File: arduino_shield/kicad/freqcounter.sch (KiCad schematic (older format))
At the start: 11 parts, among them J1 ICSP PICKIT, J2 USB-Serial, P1 LCD_DISPLAY_16X2, U1 PIC16F18446, Y1 Crystal 8MHz

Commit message: Updated kicad schematic
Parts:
- removed P1: LCD_DISPLAY_16X2, SIL-16, symbol LCD_DISPLAY_16X2:LCD_DISPLAY_16X2
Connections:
- wire segments 40 -> 24
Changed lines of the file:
@@
 EESchema Schematic File Version 4
-LIBS:freqcounter_16F18446-cache
+LIBS:freqcounter-cache
 EELAYER 26 0
 EELAYER END
@@
 Wire Wire Line
 	5500 2700 6900 2700
-$Comp
-L LCD_DISPLAY_16X2:LCD_DISPLAY_16X2 P1
-U 1 1 5EA1FBB9
-P 4200 4650
-F 0 "P1" H 6533 4550 50  0000 L CNN
-F 1 "LCD_DISPLAY_16X2" H 6533 4457 50  0000 L CNN
-F 2 "SIL-16" H 6533 4364 50  0000 L CNN
-F 3 "" H 4200 4650 50  0001 C CNN
-	1    4200 4650
-	1    0    0    -1
-$EndComp
 Text GLabel 5500 3000 2    40   Input ~ 0
 LCD_RS
 Text GLabel 5500 3100 2    40   Input ~ 0
 LCD_E
-Text GLabel 4700 4400 1    40   Input ~ 0
-LCD_E
-Text GLabel 4500 4400 1    40   Input ~ 0
-LCD_RS
-Wire Wire Line
-	4600 4400 4600 4100
-Wire Wire Line
-	4600 4100 4800 4100
-Wire Wire Line
-	4800 4100 4800 4400
-Wire Wire Line
-	4800 4100 4900 4100
-Wire Wire Line
-	4900 4100 4900 4400
-Connection ~ 4800 4100
-Wire Wire Line
-	4900 4100 5000 4100
-Wire Wire Line
-	5000 4100 5000 4400
-Connection ~ 4900 4100
-Wire Wire Line
-	5000 4100 5100 4100
-Wire Wire Line
-	5100 4100 5100 4400
-Connection ~ 5000 4100
-Text GLabel 4600 4000 1    40   Input ~ 0
-GND
-Wire Wire Line
-	4600 4100 4600 4000
-Connection ~ 4600 4100
-Wire Wire Line
-	4600 4100 4400 4100
-Wire Wire Line
-	4400 4100 4400 4400
-Wire Wire Line
-	5100 4100 5700 4100
-Wire Wire Line
-	5700 4100 5700 4400
-Connection ~ 5100 4100
 Text GLabel 5500 3200 2    40   Input ~ 0
 LCD_D4
@@
 Text GLabel 4500 3200 0    40   Input ~ 0
 LCD_D6
-Text GLabel 5200 4400 1    40   Input ~ 0
-LCD_D4
-Text GLabel 5300 4400 1    40   Input ~ 0
-LCD_D5
-Text GLabel 5500 4400 1    40   Input ~ 0
-LCD_D7
-Text GLabel 5400 4400 1    40   Input ~ 0
-LCD_D6
-Wire Wire Line
-	4400 4100 4200 4100
-Wire Wire Line
-	4200 4100 4200 4400
-Connection ~ 4400 4100
-Text GLabel 4300 4400 1    40   Input ~ 0
-VDD
 Wire Wire Line
 	3750 2600 4500 2600

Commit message: Updated kicad schematic
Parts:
- removed J2: USB-Serial, symbol Connector:Conn_01x04_Female
- removed R11, R12: 180, Resistor_SMD:R_0805_2012Metric_Pad1.15x1.40mm_HandSolder, symbol Device:R
- removed U1: PIC16F18446, Package_SO:SOIC-20W_7.5x12.8mm_P1.27mm, symbol PIC16F18446:PIC16F18446
- removed Y1: Crystal 8MHz, Crystal:Crystal_HC18-U_Vertical, symbol Device:Crystal
- added C1: 10uF, Capacitor_SMD:C_0805_2012Metric_Pad1.15x1.40mm_HandSolder, symbol Device:C
- added C4, C5: 100nF, Capacitor_SMD:C_0805_2012Metric_Pad1.15x1.40mm_HandSolder, symbol Device:C
- added J10: I2C_2, symbol Connector:Conn_01x04_Male
- added J11: PARALEL, symbol Connector:Conn_01x08_Male
- added J2: Arduino_Power, symbol Connector:Conn_01x06_Male
- added J3: Arduino_Digital_2, symbol Connector:Conn_01x08_Male
- added J4: Arduino_Analog, symbol Connector:Conn_01x06_Male
- added J5: Arduino_Digital_1, symbol Connector:Conn_01x08_Male
- added J6: INPUT_A, symbol Connector:Conn_01x02_Male
- added J7: INPUT_B, symbol Connector:Conn_01x02_Male
- added J8: INPUT_ZCD, symbol Connector:Conn_01x02_Male
- added J9: I2C_1, symbol Connector:Conn_01x04_Male
- added R1: 10K, Resistor_SMD:R_0805_2012Metric_Pad1.15x1.40mm_HandSolder, symbol Device:R
- added R2: 180, Resistor_SMD:R_0805_2012Metric_Pad1.15x1.40mm_HandSolder, symbol Device:R
- added R4: 1M, Resistor_SMD:R_0805_2012Metric_Pad1.15x1.40mm_HandSolder, symbol Device:R
- added U1: PIC16F18446, symbol freqcounter:PIC16F18446
- added U2: TCXO, symbol freqcounter:TCXO
- renumbered C5 to C2, C1 to C3, R1 to R3
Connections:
- net labels added: 3.3V, 32MHz, 5V, ARD_RX, ARD_TX, ARD_VIN, AREF, P0, P1, P2, P3, RESET, SCL, SDA
- net labels removed: LCD_D4, LCD_D5, LCD_D6, LCD_D7, LCD_E, LCD_RS, RX, TX
- wire segments 24 -> 53
- no-connect marks 0 -> 1
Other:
- note added: "ARDUINO INTERFACE"
- moved on the sheet: D1, J1, R3

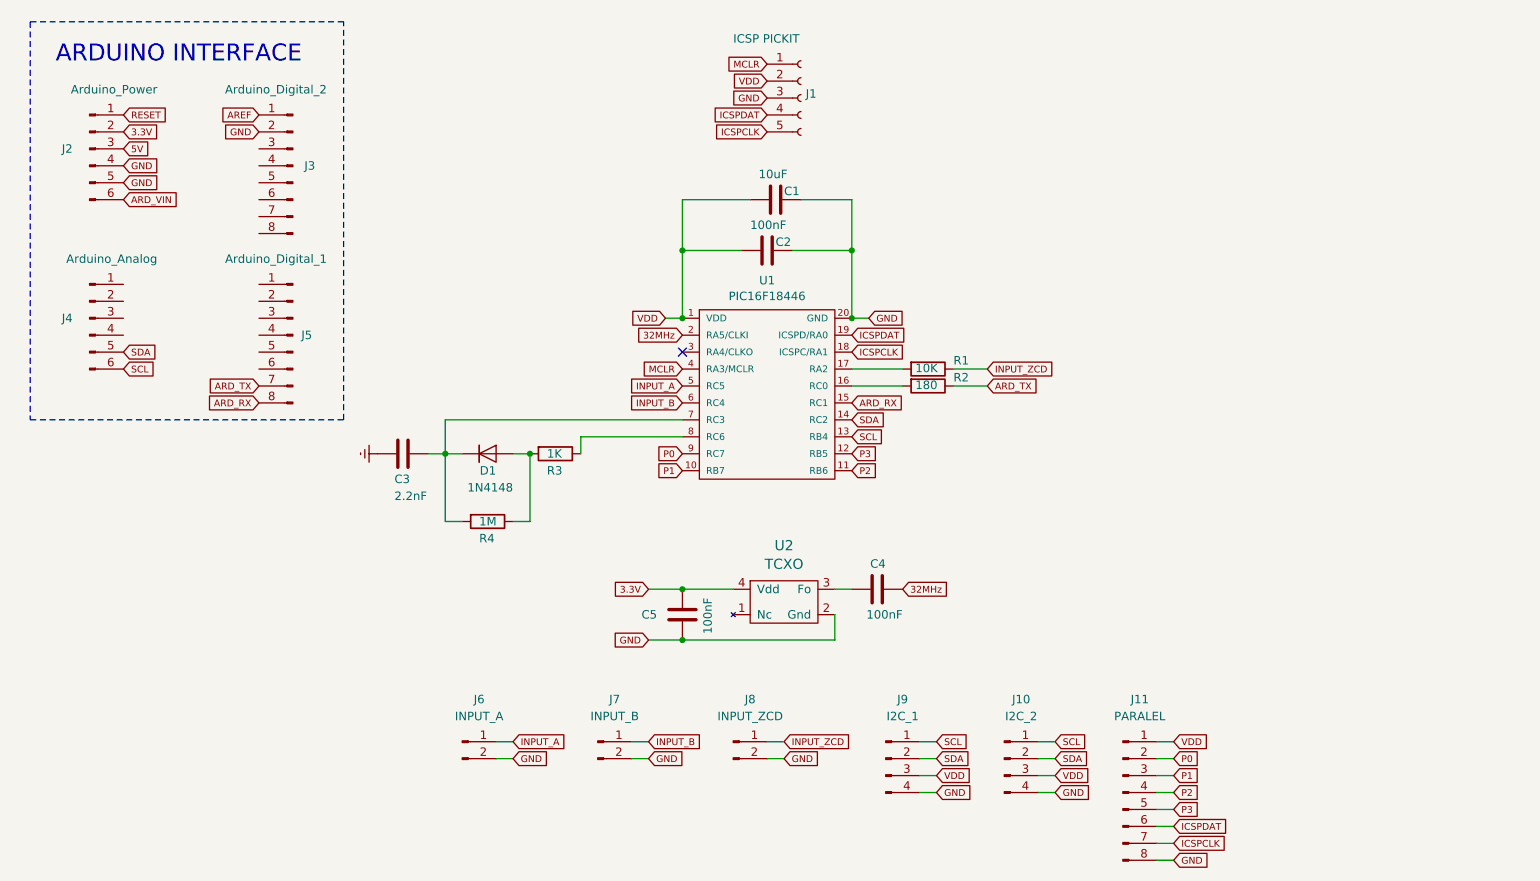
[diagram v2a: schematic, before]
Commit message: Updated Arduino shield schematic and PCB
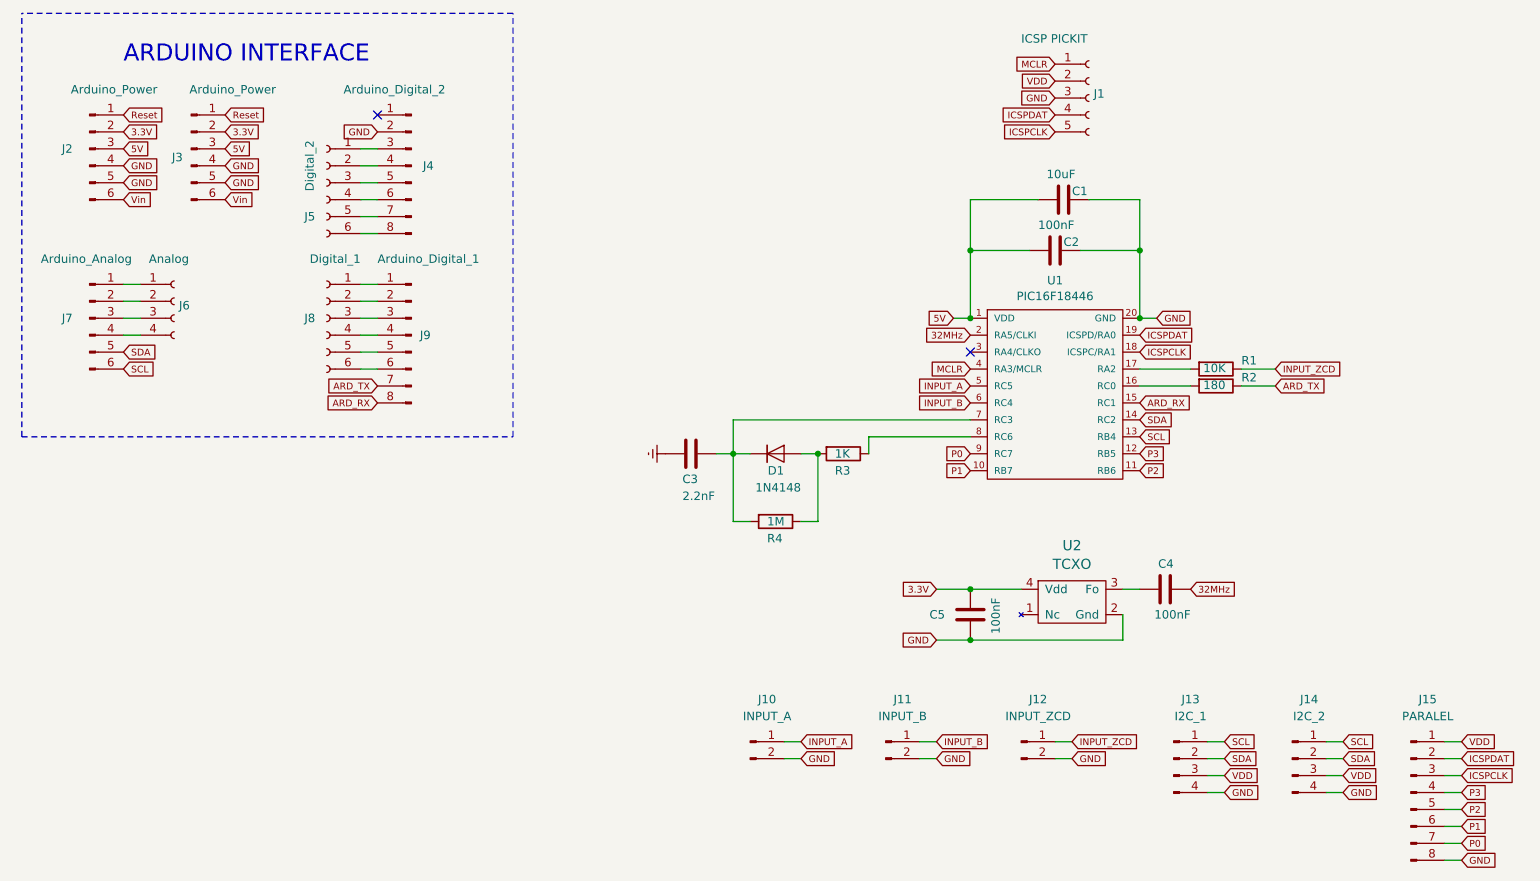
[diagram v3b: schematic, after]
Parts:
- added J3: Arduino_Power, Footprints:Connector_1x06, symbol Connector:Conn_01x06_Male
- added J5: Digital_2, Footprints:Connector_1x06, symbol Connector:Conn_01x06_Female
- added J6: Analog, Footprints:Connector_1x04, symbol Connector:Conn_01x04_Female
- added J8: Digital_1, Footprints:Connector_1x06, symbol Connector:Conn_01x06_Female
- J1: footprint (none) -> Connector_PinHeader_2.54mm:PinHeader_1x05_P2.54mm_Vertical
- J10: renamed from J6; footprint (none) -> Connector_PinHeader_2.54mm:PinHeader_1x02_P2.54mm_Vertical
- J11: renamed from J7; footprint (none) -> Connector_PinHeader_2.54mm:PinHeader_1x02_P2.54mm_Vertical
- J12: renamed from J8; footprint (none) -> Connector_PinHeader_2.54mm:PinHeader_1x02_P2.54mm_Vertical
- J13: renamed from J9; footprint (none) -> Connector_PinHeader_2.54mm:PinHeader_1x04_P2.54mm_Vertical
- J14: renamed from J10; footprint (none) -> Connector_PinHeader_2.54mm:PinHeader_1x04_P2.54mm_Vertical
- J15: renamed from J11; footprint (none) -> Footprints:Connector_1x08
- J2: footprint (none) -> Footprints:Connector_1x06
- J4: renamed from J3; footprint (none) -> Footprints:Connector_1x08
- J7: renamed from J4; footprint (none) -> Footprints:Connector_1x06
- J9: renamed from J5; footprint (none) -> Footprints:Connector_1x08
- U1: footprint (none) -> Package_SO:SOIC-20W_7.5x12.8mm_P1.27mm
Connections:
- net 3.3V: now also J3.2 (Pin_2)
- net 5V: now also C1.2, C2.2, U1.1 (VDD), J3.3 (Pin_3)
- net GND: now also J3.4 (Pin_4), J3.5 (Pin_5)
- net ICSPCLK: now also J15.3 (Pin_3); no longer J15.7 (Pin_7)
- net ICSPDAT: now also J15.2 (Pin_2); no longer J15.6 (Pin_6)
- net P0: now also J15.7 (Pin_7); no longer J15.2 (Pin_2)
- net P1: now also J15.6 (Pin_6); no longer J15.3 (Pin_3)
- net P2: now also J15.5 (Pin_5); no longer J15.4 (Pin_4)
- net P3: now also J15.4 (Pin_4); no longer J15.5 (Pin_5)
- net VDD: no longer C1.2, C2.2, U1.1 (VDD)
- net at J4.3 (Pin_3): now also J5.1 (Pin_1)
- net at J4.4 (Pin_4): now also J5.2 (Pin_2)
- net at J4.5 (Pin_5): now also J5.3 (Pin_3)
- net at J4.6 (Pin_6): now also J5.4 (Pin_4)
- net at J4.7 (Pin_7): now also J5.5 (Pin_5)
- net at J4.8 (Pin_8): now also J5.6 (Pin_6)
- net at J9.1 (Pin_1): now also J8.1 (Pin_1)
- net at J9.2 (Pin_2): now also J8.2 (Pin_2)
- net at J9.3 (Pin_3): now also J8.3 (Pin_3)
- net at J9.4 (Pin_4): now also J8.4 (Pin_4)
- net at J9.5 (Pin_5): now also J8.5 (Pin_5)
- net at J9.6 (Pin_6): now also J8.6 (Pin_6)
- net at J7.1 (Pin_1): now also J6.1 (Pin_1)
- net at J7.2 (Pin_2): now also J6.2 (Pin_2)
- net at J7.3 (Pin_3): now also J6.3 (Pin_3)
- net at J7.4 (Pin_4): now also J6.4 (Pin_4)
- net ARD_VIN renamed Vin
- net Vin: now also J3.6 (Pin_6)
- net AREF: no longer names the net of J4.1 (Pin_1)
- net RESET renamed Reset
- net Reset: now also J3.1 (Pin_1)
- no-connect marks 1 -> 2
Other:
- moved on the sheet: C1, C2, C3, C4, C5, D1, J1, J10, J11, J12, J13, J14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

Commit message: Updated Schematic and PCB
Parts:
- added R5, R6: 10K, Resistor_SMD:R_0805_2012Metric_Pad1.15x1.40mm_HandSolder, symbol Device:R
- U2: footprint (none) -> Footprints:TCXO-5032
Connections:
- net SCL: now also R5.2
- net SDA: now also R6.2
- net VDD: now also R5.1, R6.1
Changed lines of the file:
@@
 F 0 "U2" H 6800 4258 60  0000 C CNN
 F 1 "TCXO" H 6800 4148 60  0000 C CNN
-F 2 "" H 6700 3950 60  0001 C CNN
+F 2 "Footprints:TCXO-5032" H 6700 3950 60  0001 C CNN
 F 3 "" H 6700 3950 60  0000 C CNN
 	1    6500 4000
@@
 Wire Notes Line
 	600  3100 600  600
+Text GLabel 8800 4100 3    40   Input ~ 0
+SCL
+Text GLabel 8900 4100 3    40   Input ~ 0
+SDA
+$Comp
+L Device:R R5
+U 1 1 5EA92C67
+P 8800 3950
+F 0 "R5" V 8750 4100 50  0000 L CNN
+F 1 "10K" V 8795 3875 50  0000 L CNN
+F 2 "Resistor_SMD:R_0805_2012Metric_Pad1.15x1.40mm_HandSolder" V 8730 3950 50  0001 C CNN
+F 3 "~" H 8800 3950 50  0001 C CNN
+	1    8800 3950
+	-1   0    0    -1
+$EndComp
+$Comp
+L Device:R R6
+U 1 1 5EA92CFB
+P 8900 3950
+F 0 "R6" V 8850 4100 50  0000 L CNN
+F 1 "10K" V 8895 3875 50  0000 L CNN
+F 2 "Resistor_SMD:R_0805_2012Metric_Pad1.15x1.40mm_HandSolder" V 8830 3950 50  0001 C CNN
+F 3 "~" H 8900 3950 50  0001 C CNN
+	1    8900 3950
+	-1   0    0    -1
+$EndComp
+Text GLabel 8800 3600 1    40   Input ~ 0
+VDD
+Wire Wire Line
+	8800 3600 8800 3650
+Wire Wire Line
+	8800 3650 8900 3650
+Wire Wire Line
+	8900 3650 8900 3800
+Connection ~ 8800 3650
+Wire Wire Line
+	8800 3650 8800 3800
 $EndSCHEMATC
